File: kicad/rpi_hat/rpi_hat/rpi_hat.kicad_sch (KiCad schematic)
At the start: 12 parts, among them J1 FrontButtons, J2 PowerButton, J3 PowerWakeup, J4 DisplaySPI, J5 BatteryLevel, J6 GPIO, Q1 AO3401A, Q2 PN2222A

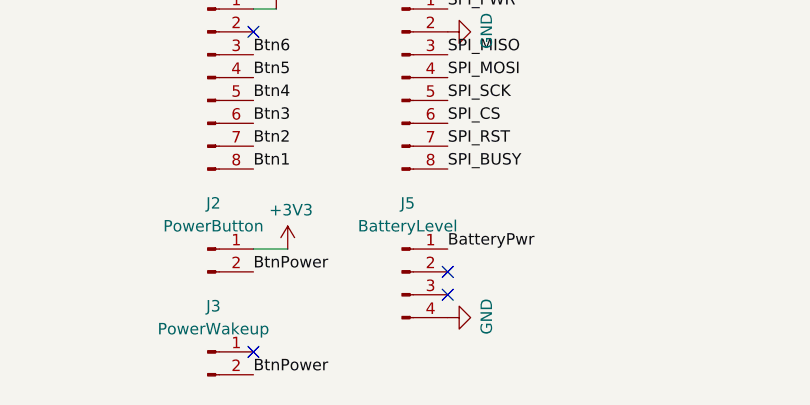
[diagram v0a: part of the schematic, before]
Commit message: Add support for power on button (#8)
* add power button

* fix bug in power on button routing in hat

* update test_buttons.py script

* implement power off buttton in all fsm

* refactor display subsystem
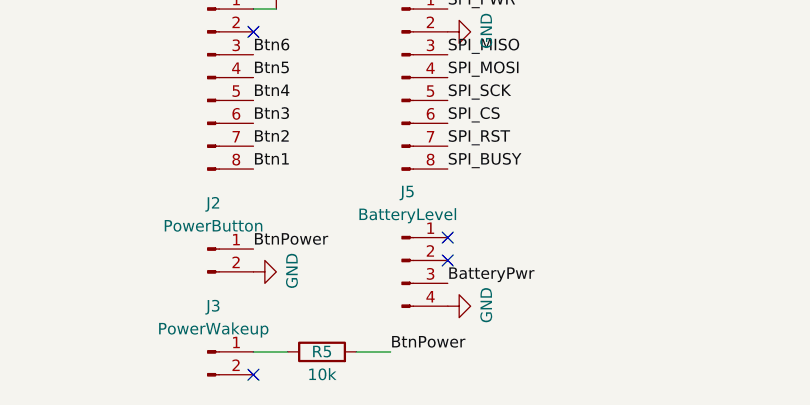
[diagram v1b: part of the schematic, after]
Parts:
- added R5: 10k, Resistor_THT:R_Axial_DIN0207_L6.3mm_D2.5mm_P10.16mm_Horizontal, symbol Device:R
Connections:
- net +3V3: no longer J2.1 (Pin_1)
- net BatteryPwr: now also J5.3 (Pin_3); no longer J5.1 (Pin_1)
- net BtnPower: now also J2.1 (Pin_1), R5.2; no longer J2.2 (Pin_2), J3.2 (Pin_2)
- net GND: now also J2.2 (Pin_2)
- net at J3.1 (Pin_1): now also R5.1
